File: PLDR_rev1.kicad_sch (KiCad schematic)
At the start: 0 parts

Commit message: Added conceptual overview schematic. Added BatteryIncoming schematic.
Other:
- title: (none) -> Conceptual Overview

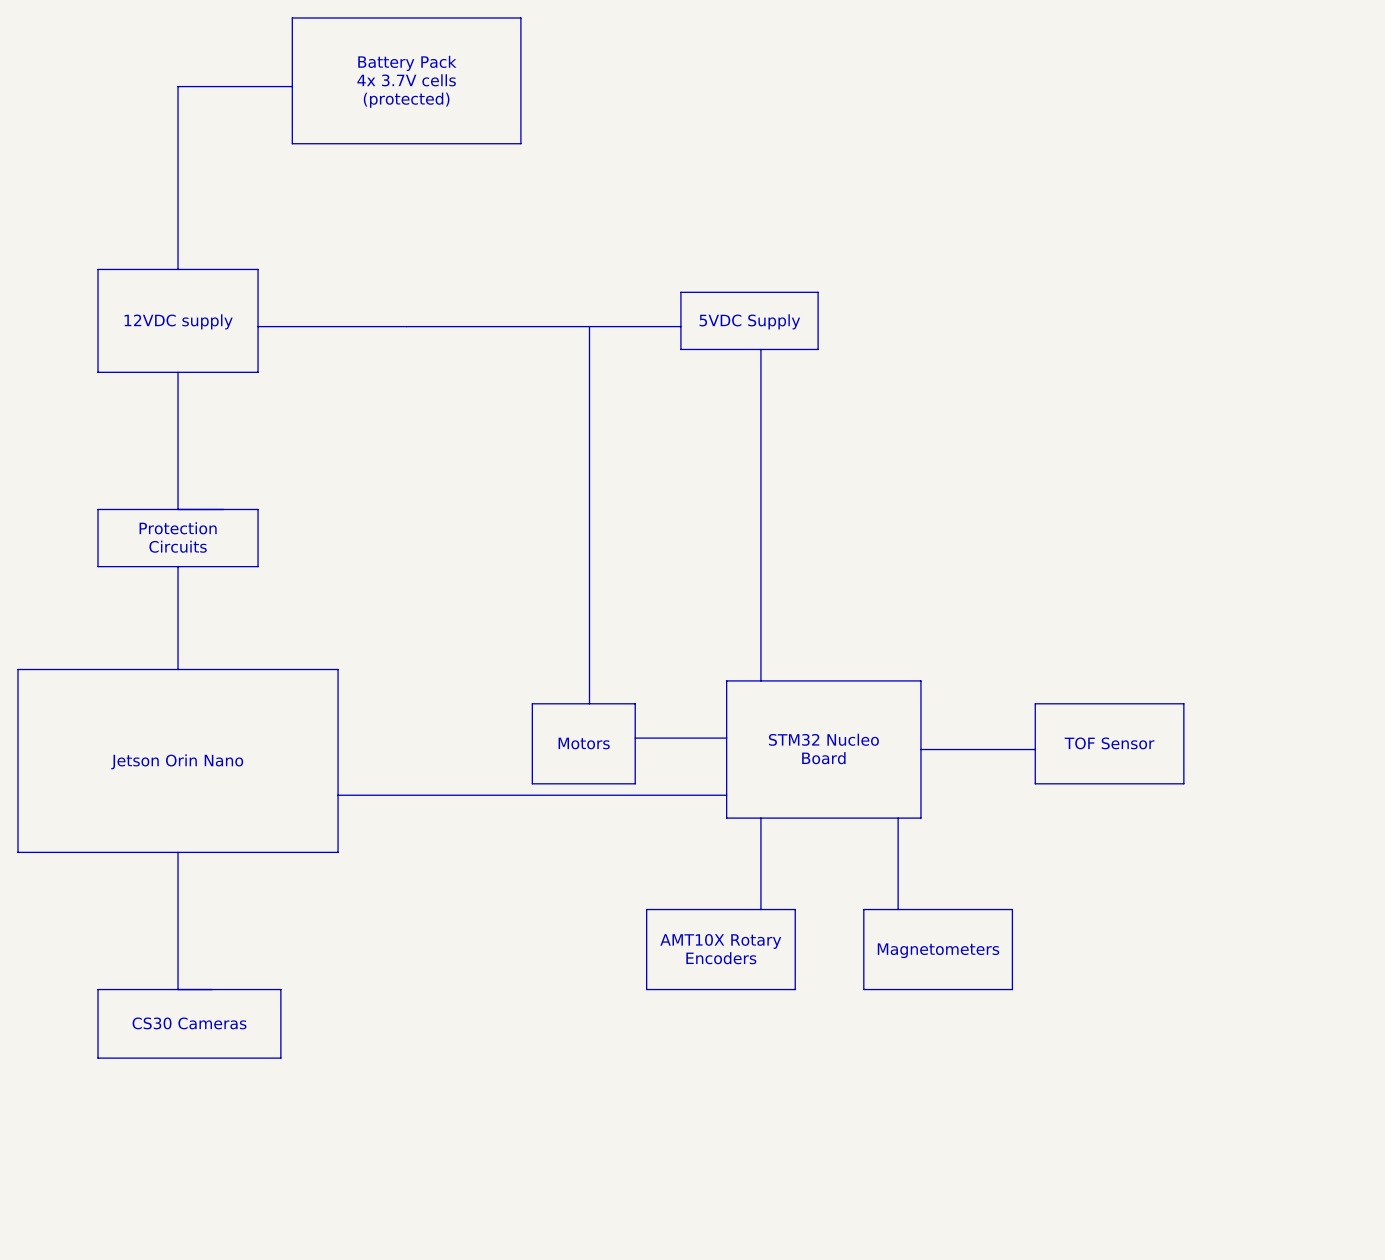
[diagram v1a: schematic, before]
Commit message: - Added new battery incomer schematic sheet. - Updated title block to include SEED Lab uAlberta
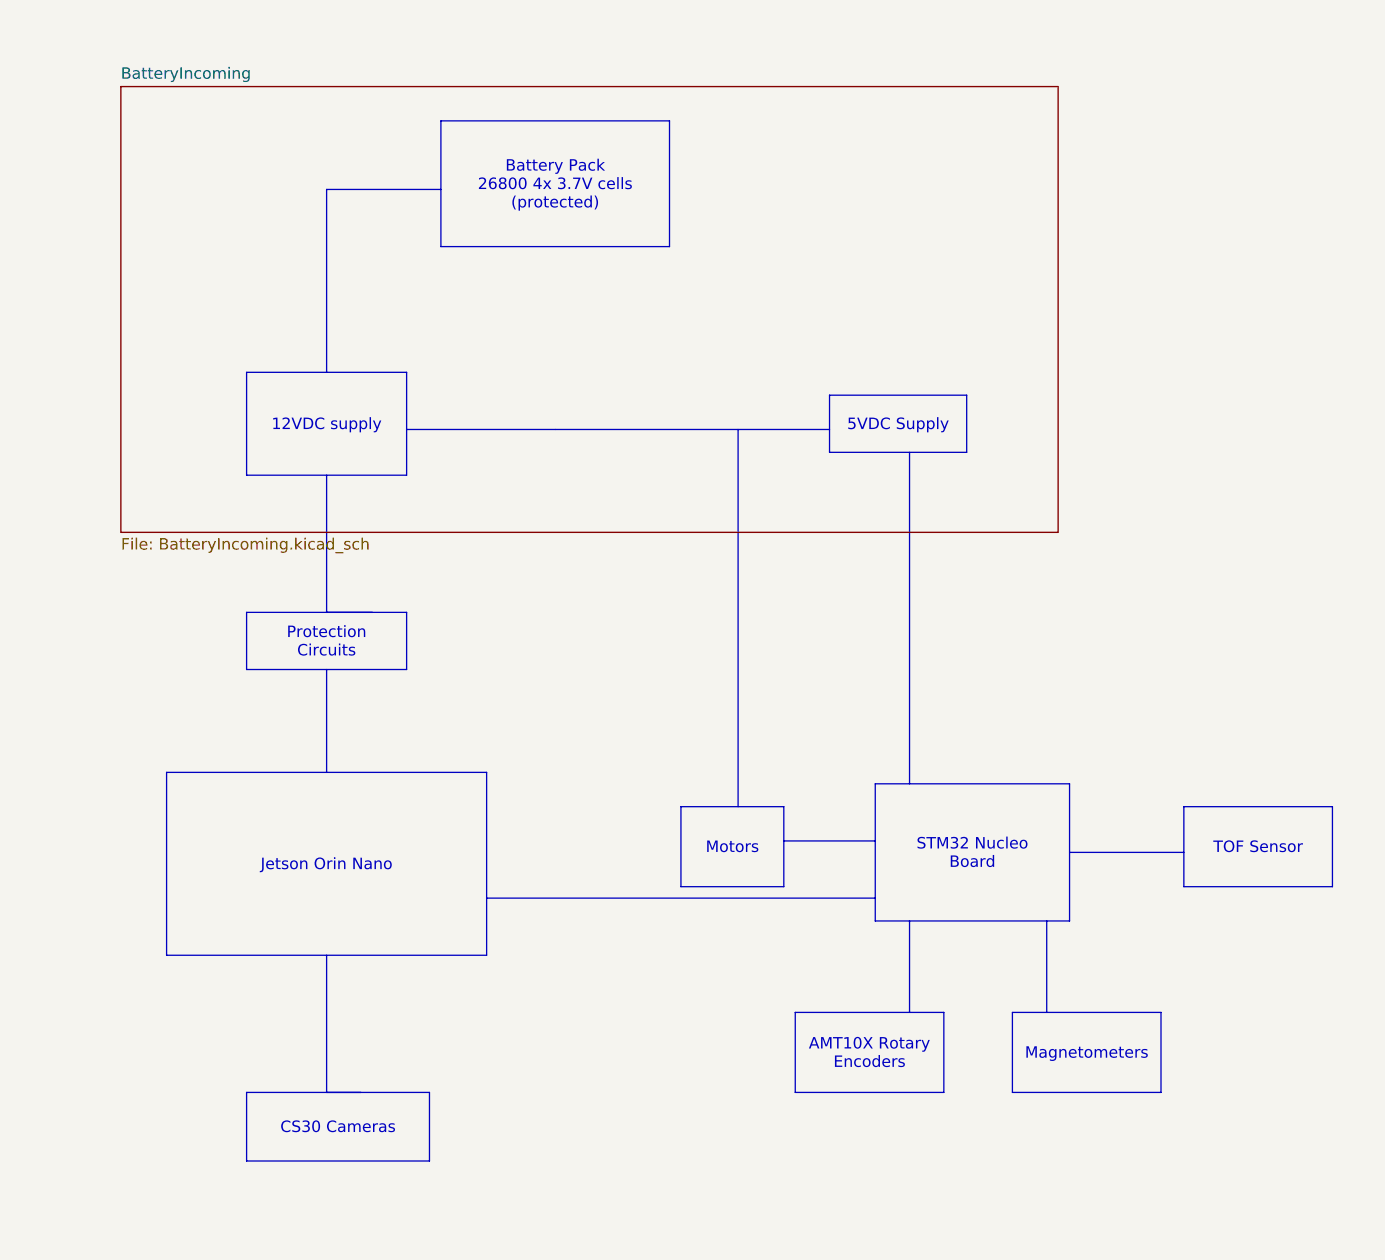
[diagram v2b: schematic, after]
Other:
- added sheet BatteryIncoming (BatteryIncoming.kicad_sch)
- company: (none) -> SEED Lab University of Alberta
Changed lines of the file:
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@@
 		(date "2026-06-09")
 		(rev "0")
+		(company "SEED Lab University of Alberta")
 	)
 	(text_box "Magnetometers"
 		(exclude_from_sim no)
-		(at 132.08 118.11 0)
+		(at 148.59 129.54 0)
 		(size 16.51 8.89)
 		(margins 0.9525 0.9525 0.9525 0.9525)
@@
 	(text_box "CS30 Cameras"
 		(exclude_from_sim no)
-		(at 46.99 127 0)
+		(at 63.5 138.43 0)
 		(size 20.32 7.62)
 		(margins 0.9525 0.9525 0.9525 0.9525)
@@
 	(text_box "12VDC supply"
 		(exclude_from_sim no)
-		(at 46.99 46.99 0)
+		(at 63.5 58.42 0)
 		(size 17.78 11.43)
 		(margins 0.9525 0.9525 0.9525 0.9525)
@@
 	(text_box "Motors"
 		(exclude_from_sim no)
-		(at 95.25 95.25 0)
+		(at 111.76 106.68 0)
 		(size 11.43 8.89)
 		(margins 0.9525 0.9525 0.9525 0.9525)
@@
 	(text_box ""
 		(exclude_from_sim no)
-		(at 76.2 26.67 0)
+		(at 92.71 38.1 0)
 		(size 0 0)
 		(margins 0.9525 0.9525 0.9525 0.9525)
@@
 	(text_box "Protection Circuits"
 		(exclude_from_sim no)
-		(at 46.99 73.66 0)
+		(at 63.5 85.09 0)
 		(size 17.78 6.35)
 		(margins 0.9525 0.9525 0.9525 0.9525)
@@
 	(text_box "AMT10X Rotary Encoders"
 		(exclude_from_sim no)
-		(at 107.95 118.11 0)
+		(at 124.46 129.54 0)
 		(size 16.51 8.89)
 		(margins 0.9525 0.9525 0.9525 0.9525)
@@
 	(text_box "TOF Sensor"
 		(exclude_from_sim no)
-		(at 151.13 95.25 0)
+		(at 167.64 106.68 0)
 		(size 16.51 8.89)
 		(margins 0.9525 0.9525 0.9525 0.9525)
@@
 	(text_box "STM32 Nucleo Board"
 		(exclude_from_sim no)
-		(at 116.84 92.71 0)
+		(at 133.35 104.14 0)
 		(size 21.59 15.24)
 		(margins 0.9525 0.9525 0.9525 0.9525)
@@
 	(text_box "5VDC Supply"
 		(exclude_from_sim no)
-		(at 111.76 49.53 0)
+		(at 128.27 60.96 0)
 		(size 15.24 6.35)
 		(margins 0.9525 0.9525 0.9525 0.9525)
@@
 	(text_box "Jetson Orin Nano"
 		(exclude_from_sim no)
-		(at 38.1 91.44 0)
+		(at 54.61 102.87 0)
 		(size 35.56 20.32)
 		(margins 0.9525 0.9525 0.9525 0.9525)
@@
 		)
 	)
-	(text_box "Battery Pack\n4x 3.7V cells (protected)"
-		(exclude_from_sim no)
-		(at 68.58 19.05 0)
+	(text_box "Battery Pack\n26800 4x 3.7V cells (protected)"
+		(exclude_from_sim no)
+		(at 85.09 30.48 0)
 		(size 25.4 13.97)
 		(margins 0.9525 0.9525 0.9525 0.9525)
@@
 	(polyline
 		(pts
-			(xy 55.88 26.67) (xy 55.88 46.99)
-		)
-		(stroke
-			(width 0)
-			(type default)
-		)
-	)
-	(polyline
-		(pts
-			(xy 120.65 107.95) (xy 120.65 118.11)
-		)
-		(stroke
-			(width 0)
-			(type default)
-		)
-	)
-	(polyline
-		(pts
-			(xy 120.65 55.88) (xy 120.65 92.71)
-		)
-		(stroke
-			(width 0)
-			(type default)
-		)
-	)
-	(polyline
-		(pts
-			(xy 135.89 107.95) (xy 135.89 118.11)
-		)
-		(stroke
-			(width 0)
-			(type default)
-		)
-	)
-	(polyline
-		(pts
-			(xy 55.88 58.42) (xy 55.88 73.66)
-		)
-		(stroke
-			(width 0)
-			(type default)
-		)
-	)
-	(polyline
-		(pts
-			(xy 64.77 53.34) (xy 81.28 53.34)
-		)
-		(stroke
-			(width 0)
-			(type default)
-		)
-	)
-	(polyline
-		(pts
-			(xy 55.88 73.66) (xy 60.96 73.66)
-		)
-		(stroke
-			(width 0)
-			(type default)
-		)
-	)
-	(polyline
-		(pts
-			(xy 55.88 127) (xy 59.69 127)
-		)
-		(stroke
-			(width 0)
-			(type default)
-		)
-	)
-	(polyline
-		(pts
-			(xy 55.88 111.76) (xy 55.88 127)
-		)
-		(stroke
-			(width 0)
-			(type default)
-		)
-	)
-	(polyline
-		(pts
-			(xy 73.66 105.41) (xy 116.84 105.41)
-		)
-		(stroke
-			(width 0)
-			(type default)
-		)
-	)
-	(polyline
-		(pts
-			(xy 106.68 99.06) (xy 116.84 99.06)
-		)
-		(stroke
-			(width 0)
-			(type default)
-		)
-	)
-	(polyline
-		(pts
-			(xy 68.58 26.67) (xy 55.88 26.67)
-		)
-		(stroke
-			(width 0)
-			(type default)
-		)
-	)
-	(polyline
-		(pts
-			(xy 81.28 53.34) (xy 111.76 53.34)
-		)
-		(stroke
-			(width 0)
-			(type default)
-		)
-	)
-	(polyline
-		(pts
-			(xy 55.88 80.01) (xy 55.88 91.44)
-		)
-		(stroke
-			(width 0)
-			(type default)
-		)
-	)
-	(polyline
-		(pts
-			(xy 101.6 53.34) (xy 101.6 95.25)
-		)
-		(stroke
-			(width 0)
-			(type solid)
-		)
-	)
-	(polyline
-		(pts
-			(xy 138.43 100.33) (xy 151.13 100.33)
-		)
-		(stroke
-			(width 0)
-			(type default)
-		)
-	)
+			(xy 72.39 38.1) (xy 72.39 58.42)
+		)
+		(stroke
+			(width 0)
+			(type default)
+		)
+	)
+	(polyline
+		(pts
+			(xy 137.16 119.38) (xy 137.16 129.54)
+		)
+		(stroke
+			(width 0)
+			(type default)
+		)
+	)
+	(polyline
+		(pts
+			(xy 137.16 67.31) (xy 137.16 104.14)
+		)
+		(stroke
+			(width 0)
+			(type default)
+		)
+	)
+	(polyline
+		(pts
+			(xy 152.4 119.38) (xy 152.4 129.54)
+		)
+		(stroke
+			(width 0)
+			(type default)
+		)
+	)
+	(polyline
+		(pts
+			(xy 72.39 69.85) (xy 72.39 85.09)
+		)
+		(stroke
+			(width 0)
+			(type default)
+		)
+	)
+	(polyline
+		(pts
+			(xy 81.28 64.77) (xy 97.79 64.77)
+		)
+		(stroke
+			(width 0)
+			(type default)
+		)
+	)
+	(polyline
+		(pts
+			(xy 72.39 85.09) (xy 77.47 85.09)
+		)
+		(stroke
+			(width 0)
+			(type default)
+		)
+	)
+	(polyline
+		(pts
+			(xy 72.39 138.43) (xy 76.2 138.43)
+		)
+		(stroke
+			(width 0)
+			(type default)
+		)
+	)
+	(polyline
+		(pts
+			(xy 72.39 123.19) (xy 72.39 138.43)
+		)
+		(stroke
+			(width 0)
+			(type default)
+		)
+	)
+	(polyline
+		(pts
+			(xy 90.17 116.84) (xy 133.35 116.84)
+		)
+		(stroke
+			(width 0)
+			(type default)
+		)
+	)
+	(polyline
+		(pts
+			(xy 123.19 110.49) (xy 133.35 110.49)
+		)
+		(stroke
+			(width 0)
+			(type default)
+		)
+	)
+	(polyline
+		(pts
+			(xy 85.09 38.1) (xy 72.39 38.1)
+		)
+		(stroke
+			(width 0)
+			(type default)
+		)
+	)
+	(polyline
+		(pts
+			(xy 97.79 64.77) (xy 128.27 64.77)
+		)
+		(stroke
+			(width 0)
+			(type default)
+		)
+	)
+	(polyline
+		(pts
+			(xy 72.39 91.44) (xy 72.39 102.87)
+		)
+		(stroke
+			(width 0)
+			(type default)
+		)
+	)
+	(polyline
+		(pts
+			(xy 118.11 64.77) (xy 118.11 106.68)
+		)
+		(stroke
+			(width 0)
+			(type solid)
+		)
+	)
+	(polyline
+		(pts
+			(xy 154.94 111.76) (xy 167.64 111.76)
+		)
+		(stroke
+			(width 0)
+			(type default)
+		)
+	)
+	(sheet
+		(at 49.53 26.67)
+		(size 104.14 49.53)
+		(exclude_from_sim no)
+		(in_bom yes)
+		(on_board yes)
+		(dnp no)
+		(fields_autoplaced yes)
+		(stroke
+			(width 0.1524)
+			(type solid)
+		)
+		(fill
+			(color 0 0 0 0)
+		)
+		(property "Sheetname" "BatteryIncoming"
+			(at 49.53 25.9584 0)
+			(show_name no)
+			(do_not_autoplace no)
+			(effects
+				(font
+					(size 1.27 1.27)
+				)
+				(justify left bottom)
+			)
+		)
+		(property "Sheetfile" "BatteryIncoming.kicad_sch"
+			(at 49.53 76.7846 0)
+			(show_name no)
+			(do_not_autoplace no)
+			(effects
+				(font
+					(size 1.27 1.27)
+				)
+				(justify left top)
+			)
+		)
+		(instances
+			(project "PLDR_rev1"
+				(path "/044e3193-aa4e-4ad4-a125-51ae4829b9ed"
+					(page "2")
+				)
+			)
+		)
+	)

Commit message: Made new library for all sensors connected to MCU (no motors)
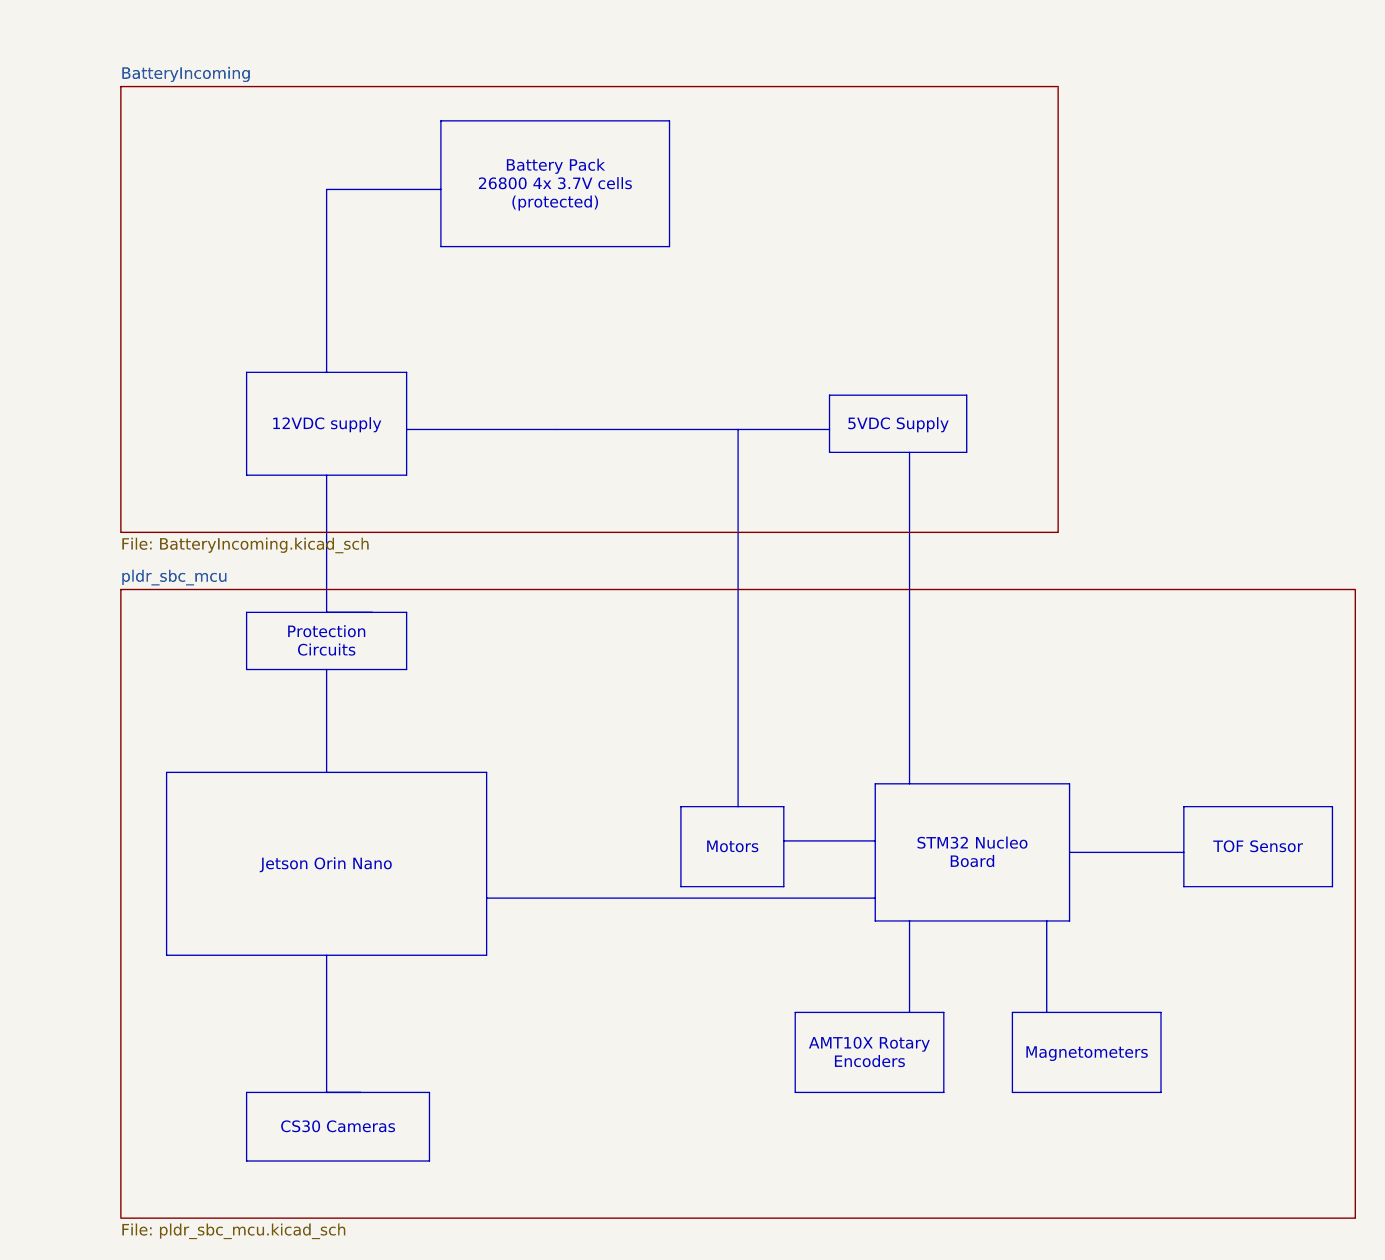
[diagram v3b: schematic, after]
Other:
- added sheet pldr_sbc_mcu (pldr_sbc_mcu.kicad_sch)
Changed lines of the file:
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@@
+		)
+	)
+	(sheet
+		(at 49.53 82.55)
+		(size 137.16 69.85)
+		(exclude_from_sim no)
+		(in_bom yes)
+		(on_board yes)
+		(dnp no)
+		(fields_autoplaced yes)
+		(stroke
+			(width 0.1524)
+			(type solid)
+		)
+		(fill
+			(color 0 0 0 0)
+		)
+		(property "Sheetname" "pldr_sbc_mcu"
+			(at 49.53 81.8384 0)
+			(show_name no)
+			(do_not_autoplace no)
+			(effects
+				(font
+					(size 1.27 1.27)
+				)
+				(justify left bottom)
+			)
+		)
+		(property "Sheetfile" "pldr_sbc_mcu.kicad_sch"
+			(at 49.53 152.9846 0)
+			(show_name no)
+			(do_not_autoplace no)
+			(effects
+				(font
+					(size 1.27 1.27)
+				)
+				(justify left top)
+			)
+		)
+		(instances
+			(project "PLDR_rev1"
+				(path "/044e3193-aa4e-4ad4-a125-51ae4829b9ed"
+					(page "3")
+				)
+			)
 		)
 	)
